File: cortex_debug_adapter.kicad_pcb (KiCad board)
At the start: 2 copper layers, 2 parts, among them J1 Conn_02x05_Odd_Even, J2 Conn_01x07_Male

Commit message: PCB done
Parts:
- added kibuzzard-62A19C5B: G***, kibuzzard-62A19C5B, B.Cu at (153.6, 100.6)
- moved J2 8.70 mm to (160.8, 93.0)
- moved J1 8.00 mm to (147.3, 98.0)
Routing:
- net VCC: track 0.00 -> 15.6 mm
- net /RESET: track 0.00 -> 14.3 mm
- net /TDI: track 0.00 -> 13.8 mm
- net /TDO/SWO: track 0.00 -> 13.3 mm
- net /TCLK/SWCLK: track 0.00 -> 12.8 mm
- net /TMS/SWDIO: track 0.00 -> 12.2 mm
- added copper zone on B.Cu, net GND
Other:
- board outline added: 19.8 x 19.2 mm
- board text added: "Designed by"
- board text added: "GND"
- board text added: "RST"
- board text added: "SWCLK/TCK"
- board text added: "SWD/JTAG adapter"
- board text added: "SWDIO/TMS"
- board text added: "SWO/TDO"
- board text added: "TDI"
- board text added: "VCC"

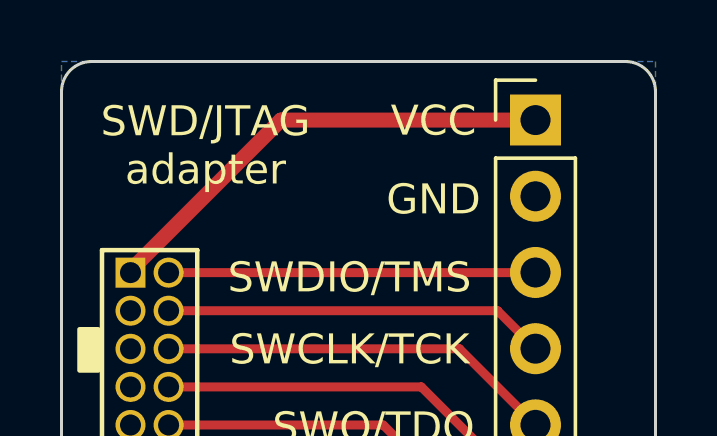
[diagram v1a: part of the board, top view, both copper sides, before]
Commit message: Finished PCB silkscreen
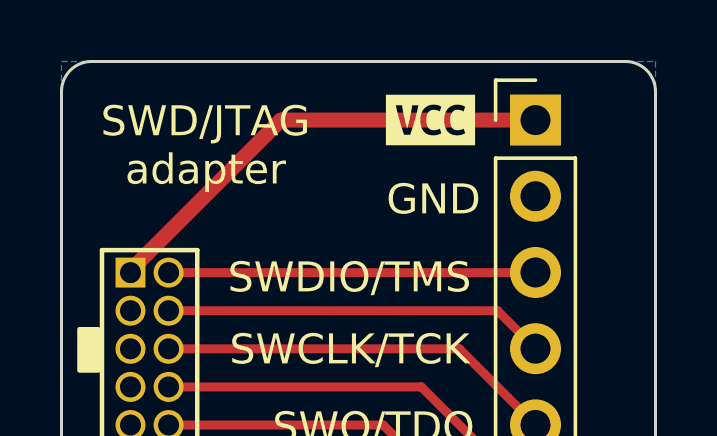
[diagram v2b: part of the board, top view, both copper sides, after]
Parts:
- added G***: LOGO, LOGO, B.Cu at (152.2, 100.6)
- added kibuzzard-630691B0: G***, kibuzzard-630691B0, F.Cu at (157.3, 93.0)
- moved kibuzzard-62A19C5B 2.30 mm to (155.9, 100.6)
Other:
- board text added: "8/22"
- board text added: "rev0.1"
- board text removed: "VCC"

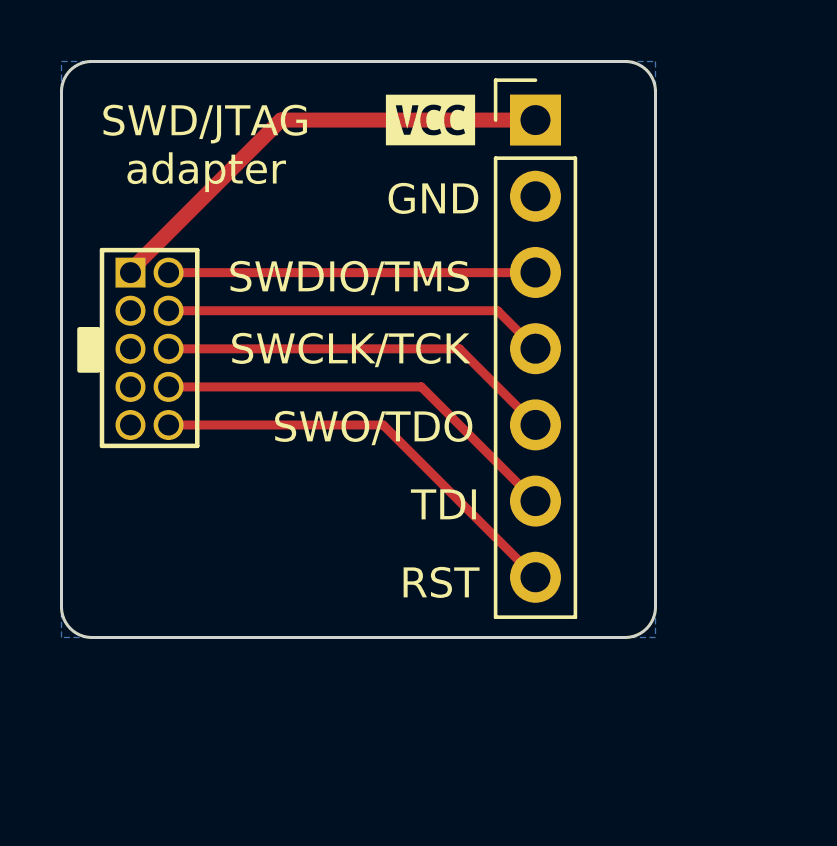
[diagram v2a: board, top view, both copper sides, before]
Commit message: Redesign because of better connector orientation
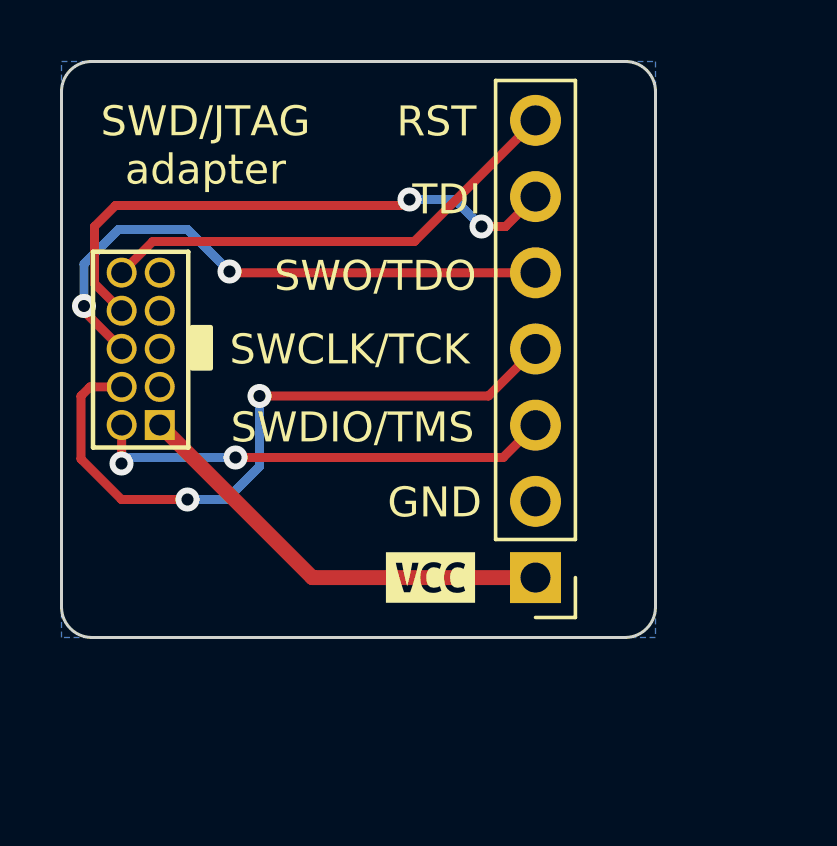
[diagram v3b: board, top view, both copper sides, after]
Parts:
- moved J2 15.2 mm to (160.8, 108.2), turned to 180 degrees
- moved kibuzzard-630691B0 15.2 mm to (157.3, 108.2)
- moved G*** 7.53 mm to (148.2, 94.2)
- moved J1 5.17 mm to (148.3, 103.1), turned to 0 degrees
- moved kibuzzard-62A19C5B 1.80 mm to (154.1, 100.6)
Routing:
- net /TCLK/SWCLK: track 12.8 -> 22.7 mm, vias 0 -> 2
- net /TDO/SWO: track 13.3 -> 19.5 mm, vias 0 -> 2
- net /TDI: track 13.8 -> 19.0 mm, vias 0 -> 2
- net /TMS/SWDIO: track 12.2 -> 15.6 mm, vias 0 -> 2
- net /RESET: track 14.3 -> 15.9 mm
- net VCC: track 15.6 -> 14.6 mm
